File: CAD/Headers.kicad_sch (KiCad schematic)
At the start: 62 parts, among them J1 SWD, J10 OUT_0, J11 OUT_1, J12 OUT_2, J13 TEMP_0, J14 TEMP_1, J15 TEMP_2, J16 EXPANSION, J17 ESP_DB, J18 250-502/000-006, J19 A2543WV-5P, J2 A2543WV-2P, J20 IO_1, J21 IO_2, J22 A2543WV-2P, J23 CAN_1_OUT, J24 DRIVER_2, J25 DRIVER_1, J26 DRIVER_0, J28 SPI_DB, J3 OUT_6, J30 LASER/VFD, J31 IO_3, J33 A2543WV-4P, J34 A2543WV-4P, J35 DRIVER_3, J36 DRIVER_4, J37 DRIVER_5, J38 CAN_0_OUT, J39 PANELDUE_SD, J4 OUT_7, J41 TEMP_3, J42 DS_LED, J44 IO_7_ISO_OUT, J47 IO_8_ISO_OUT, J48 SBC, J49 A2543WV-2P, J5 OUT_8, J50 EXT_5V_IN, J51 IO_4, J53 IO_5, J54 IO_6, J55 IO_7, J56 IO_8, J59 A2543WV-2P, J6 OUT_3, J60 A2543WV-2P, J61 IO_7_ISO_IN, J62 IO_8_ISO_IN, J7 OUT_4, J8 OUT_5

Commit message: Fix Part Name
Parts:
- J18: value 250-502/000-006 -> 250-202/000-006; footprint 3DPotter:CONN2_250-502&slash_000-006_WAG -> 3DPotter:CONN2_250-202&slash_000-006_WAG; LCSC (none) -> C2765061
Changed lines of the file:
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@@
 			)
 		)
-		(property "Value" "250-502/000-006"
+		(property "Value" "250-202/000-006"
 			(at 53.34 26.6699 0)
 			(effects
@@
 			)
 		)
-		(property "Footprint" "3DPotter:CONN2_250-502&slash_000-006_WAG"
+		(property "Footprint" "3DPotter:CONN2_250-202&slash_000-006_WAG"
 			(at 48.006 30.226 0)
 			(effects
@@
 			)
 		)
-		(property "Datasheet" "250-502/000-006"
+		(property "Datasheet" "250-202/000-006"
 			(at 48.514 34.29 0)
 			(effects
@@
 				)
 				(hide yes)
+			)
+		)
+		(property "LCSC" "C2765061"
+			(at 39.37 24.13 0)
+			(effects
+				(font
+					(size 1.524 1.524)
+				)
+				(hide yes)

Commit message: Wago confuses me
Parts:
- J18: value 250-202/000-006 -> 250-502/000-006; footprint 3DPotter:CONN2_250-202&slash_000-006_WAG -> 3DPotter:CONN2_250-502&slash_000-006_WAG; LCSC C2765061 -> C3309714
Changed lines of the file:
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@@
 			)
 		)
-		(property "Value" "250-202/000-006"
+		(property "Value" "250-502/000-006"
 			(at 53.34 26.6699 0)
 			(effects
@@
 			)
 		)
-		(property "Footprint" "3DPotter:CONN2_250-202&slash_000-006_WAG"
+		(property "Footprint" "3DPotter:CONN2_250-502&slash_000-006_WAG"
 			(at 48.006 30.226 0)
 			(effects
@@
 			)
 		)
-		(property "Datasheet" "250-202/000-006"
+		(property "Datasheet" "250-502/000-006"
 			(at 48.514 34.29 0)
 			(effects
@@
 			)
 		)
-		(property "LCSC" "C2765061"
+		(property "LCSC" "C3309714"
 			(at 39.37 24.13 0)
 			(effects

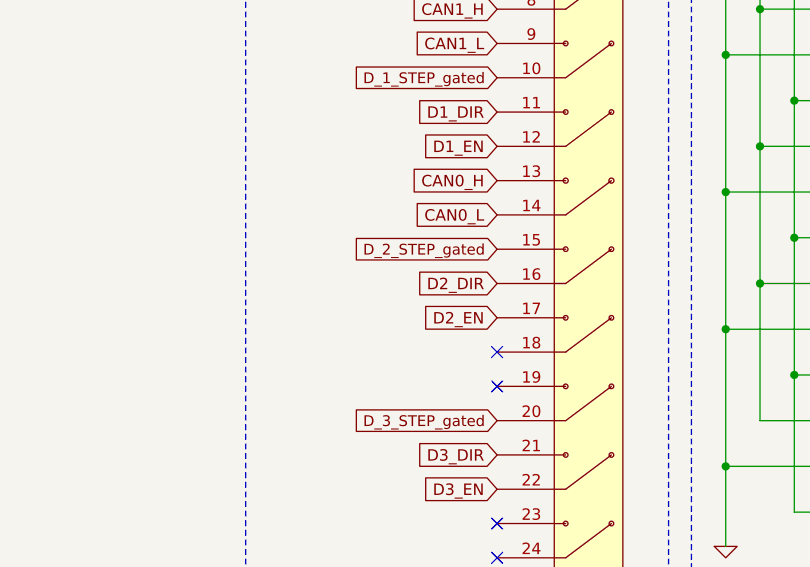
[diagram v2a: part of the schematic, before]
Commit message: Pin Changes / Misc
Changing some pins around so I have a chip select
Processor Pins:
PC28 ---> PA9 (Driver_2_Step)
PC29[AFE1_AD4] ---> PB1[AFE1_AD0] (TEMP_1)
PC28 -> spi1cs1
PC29 -> spi1cs2 (Unused as of now)
IDC Header:
CAN 0 Lines removed
13 -> SPI1_MOSI_BUFF
14 -> SP1_MISO
18 -> SPI1_SPCK_BUFF
19 -> spi1cs1
Misc:
Fixed all library links, should get a lot less errors now
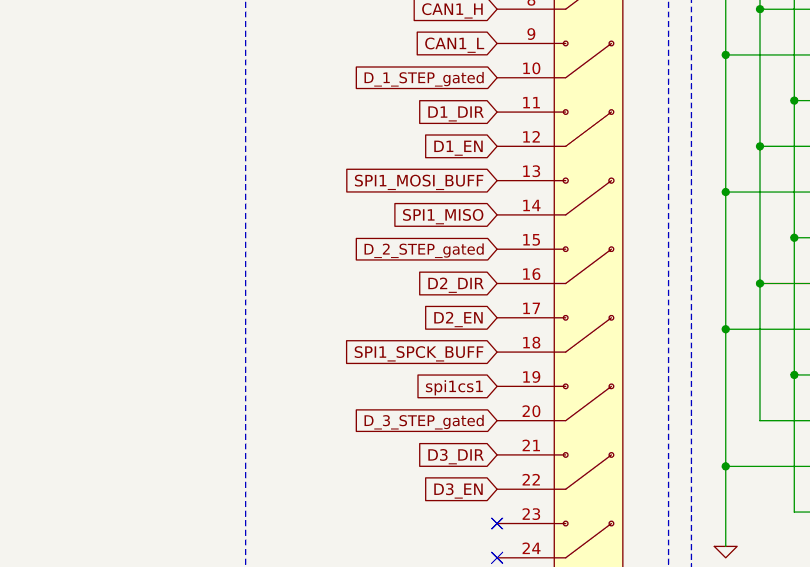
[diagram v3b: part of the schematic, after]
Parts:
- J19: footprint Connector_Molex:Wurth_61900511121-1x05_P2.54mm_Vertical(Molex_KK-254_AE-6410-05A_Compatibe) -> Connector_Molex:Molex_KK-254_AE-6410-05A_1x05_P2.54mm_Vertical
- J2, J49, J59, J60: footprint Connector_Molex:Wurth_61900211121-1x02_P2.54mm_Vertical-(Molex_KK-254_AE-6410-02Acompatible) -> Connector_Molex:Molex_KK-254_AE-6410-02A_1x02_P2.54mm_Vertical
- J30: footprint Connector_Molex:Wurth_61900311121-1x03_P2.54mm_Vertical(Molex_KK-254_AE-6410-03A_Compatible) -> Connector_Molex:Molex_KK-254_AE-6410-03A_1x03_P2.54mm_Vertical
- J33, J34: footprint Carters_Various_Bits_and_Pieces:Wurth_61900411121-1x04_P2.54mm_Vertical(1.2mm_ID) -> Connector_Molex:Molex_KK-254_AE-6410-04A_1x04_P2.54mm_Vertical
- R108: footprint Resistor_SMD:R_0603_1608Metric_Wbry -> Resistor_SMD:R_0603_1608Metric
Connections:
- net CAN0_H: no longer J16.13
- net CAN0_L: no longer J16.14
- net SPI1_MISO: now also J16.14
- net SPI1_MOSI_BUFF: now also J16.13
- net SPI1_SPCK_BUFF: now also J16.18
- net spi1cs1: now reaches J16.19
- no-connect marks 28 -> 26
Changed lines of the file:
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@@
 	)
 	(no_connect
-		(at 105.41 252.73)
-	)
-	(no_connect
 		(at 105.41 290.83)
 	)
@@
 		(at 208.915 65.405)
 	)
-	(no_connect
-		(at 105.41 256.54)
-	)
 	(wire
 		(pts
@@
 		)
 	)
+	(global_label "spi1cs1"
+		(shape input)
+		(at 105.41 256.54 180)
+		(effects
+			(font
+				(size 1.27 1.27)
+			)
+			(justify right)
+		)
+		(property "Intersheetrefs" "${INTERSHEET_REFS}"
+			(at 105.41 256.54 0)
+			(effects
+				(font
+					(size 1.27 1.27)
+				)
+				(hide yes)
+			)
+		)
+	)
 	(global_label "V_OUT_LC_1"
 		(shape input)
@@
 		)
 	)
-	(global_label "CAN0_L"
-		(shape input)
-		(at 105.41 237.49 180)
-		(fields_autoplaced yes)
-		(effects
-			(font
-				(size 1.27 1.27)
-			)
-			(justify right)
-		)
-		(property "Intersheetrefs" "${INTERSHEET_REFS}"
-			(at 96.1847 237.49 0)
-			(effects
-				(font
-					(size 1.27 1.27)
-				)
-				(justify right)
-				(hide yes)
-			)
-		)
-	)
 	(global_label "OUT_3_NEG"
 		(shape input)
@@
 		)
 	)
+	(global_label "SPI1_MISO"
+		(shape input)
+		(at 105.41 237.49 180)
+		(fields_autoplaced yes)
+		(effects
+			(font
+				(size 1.27 1.27)
+			)
+			(justify right)
+		)
+		(property "Intersheetrefs" "${INTERSHEET_REFS}"
+			(at 93.2214 237.49 0)
+			(effects
+				(font
+					(size 1.27 1.27)
+				)
+				(justify right)
+				(hide yes)
+			)
+		)
+	)
 	(global_label "D_0_ERR"
 		(shape input)
@@
 		)
 	)
+	(global_label "SPI1_MOSI_BUFF"
+		(shape input)
+		(at 105.41 233.68 180)
+		(fields_autoplaced yes)
+		(effects
+			(font
+				(size 1.27 1.27)
+			)
+			(justify right)
+		)
+		(property "Intersheetrefs" "${INTERSHEET_REFS}"
+			(at 87.4761 233.68 0)
+			(effects
+				(font
+					(size 1.27 1.27)
+				)
+				(justify right)
+				(hide yes)
+			)
+		)
+	)
 	(global_label "5V_EXT"
 		(shape input)
@@
 		)
 	)
-	(global_label "CAN0_H"
-		(shape input)
-		(at 105.41 233.68 180)
-		(fields_autoplaced yes)
-		(effects
-			(font
-				(size 1.27 1.27)
-			)
-			(justify right)
-		)
-		(property "Intersheetrefs" "${INTERSHEET_REFS}"
-			(at 95.8823 233.68 0)
-			(effects
-				(font
-					(size 1.27 1.27)
-				)
-				(justify right)
-				(hide yes)
-			)
-		)
-	)
 	(global_label "5V_EXT"
 		(shape input)
@@
 		)
 	)
+	(global_label "SPI1_SPCK_BUFF"
+		(shape input)
+		(at 105.41 252.73 180)
+		(fields_autoplaced yes)
+		(effects
+			(font
+				(size 1.27 1.27)
+			)
+			(justify right)
+		)
+		(property "Intersheetrefs" "${INTERSHEET_REFS}"
+			(at 87.0528 252.73 0)
+			(effects
+				(font
+					(size 1.27 1.27)
+				)
+				(justify right)
+				(hide yes)
+			)
+		)
+	)
 	(global_label "5V_EXT"
 		(shape input)
@@
 			)
 		)
-		(property "Footprint" "Connector_Molex:Wurth_61900211121-1x02_P2.54mm_Vertical-(Molex_KK-254_AE-6410-02Acompatible)"
+		(property "Footprint" "Connector_Molex:Molex_KK-254_AE-6410-02A_1x02_P2.54mm_Vertical"
 			(at 42.545 81.28 0)
 			(effects
@@
 			)
 		)
-		(property "Footprint" "Connector_Molex:Wurth_61900511121-1x05_P2.54mm_Vertical(Molex_KK-254_AE-6410-05A_Compatibe)"
+		(property "Footprint" "Connector_Molex:Molex_KK-254_AE-6410-05A_1x05_P2.54mm_Vertical"
 			(at 165.1 143.51 0)
 			(effects
@@
 			)
 		)
-		(property "Footprint" "Connector_Molex:Wurth_61900311121-1x03_P2.54mm_Vertical(Molex_KK-254_AE-6410-03A_Compatible)"
+		(property "Footprint" "Connector_Molex:Molex_KK-254_AE-6410-03A_1x03_P2.54mm_Vertical"
 			(at 58.42 165.735 0)
 			(effects
@@
 			)
 		)
-		(property "Footprint" "Resistor_SMD:R_0603_1608Metric_Wbry"
+		(property "Footprint" "Resistor_SMD:R_0603_1608Metric"
 			(at 46.99 162.56 0)
 			(effects
@@
 			)
 		)
-		(property "Footprint" "Connector_Molex:Wurth_61900211121-1x02_P2.54mm_Vertical-(Molex_KK-254_AE-6410-02Acompatible)"
+		(property "Footprint" "Connector_Molex:Molex_KK-254_AE-6410-02A_1x02_P2.54mm_Vertical"
 			(at 45.72 184.15 0)
 			(effects
@@
 			)
 		)
-		(property "Footprint" "Connector_Molex:Wurth_61900211121-1x02_P2.54mm_Vertical-(Molex_KK-254_AE-6410-02Acompatible)"
+		(property "Footprint" "Connector_Molex:Molex_KK-254_AE-6410-02A_1x02_P2.54mm_Vertical"
 			(at 201.93 104.14 0)
 			(effects
@@
 			)
 		)
-		(property "Footprint" "Connector_Molex:Wurth_61900211121-1x02_P2.54mm_Vertical-(Molex_KK-254_AE-6410-02Acompatible)"
+		(property "Footprint" "Connector_Molex:Molex_KK-254_AE-6410-02A_1x02_P2.54mm_Vertical"
 			(at 201.295 118.11 0)
 			(effects
@@
 			)
 		)
-		(property "Footprint" "Carters_Various_Bits_and_Pieces:Wurth_61900411121-1x04_P2.54mm_Vertical(1.2mm_ID)"
+		(property "Footprint" "Connector_Molex:Molex_KK-254_AE-6410-04A_1x04_P2.54mm_Vertical"
 			(at 238.125 100.965 0)
 			(effects
@@
 			)
 		)
-		(property "Footprint" "Carters_Various_Bits_and_Pieces:Wurth_61900411121-1x04_P2.54mm_Vertical(1.2mm_ID)"
+		(property "Footprint" "Connector_Molex:Molex_KK-254_AE-6410-04A_1x04_P2.54mm_Vertical"
 			(at 238.125 114.935 0)
 			(effects

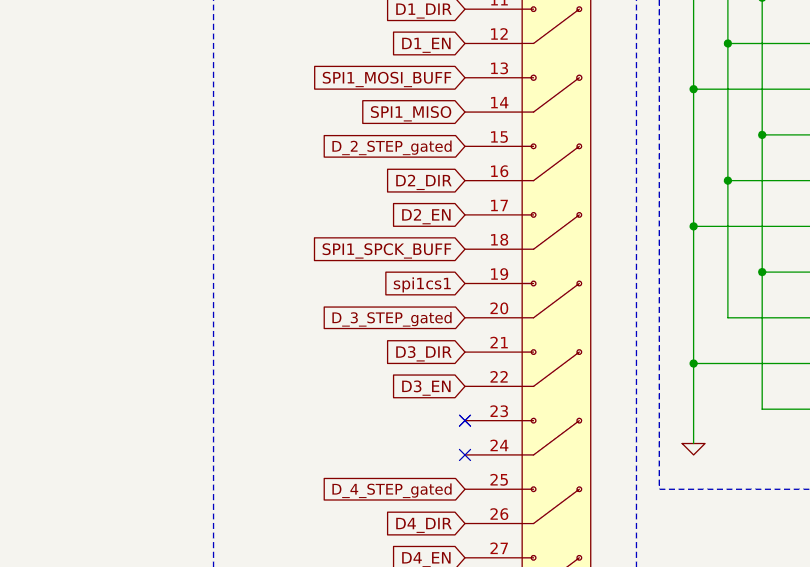
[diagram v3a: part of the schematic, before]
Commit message: Board Finished
Board has been slightly modified to add SPI to the BBC.
A lot of library mismatch/ not found errors were fixed. Only errors that exist currently are all related to the silkscreen edges on all 0402 components.
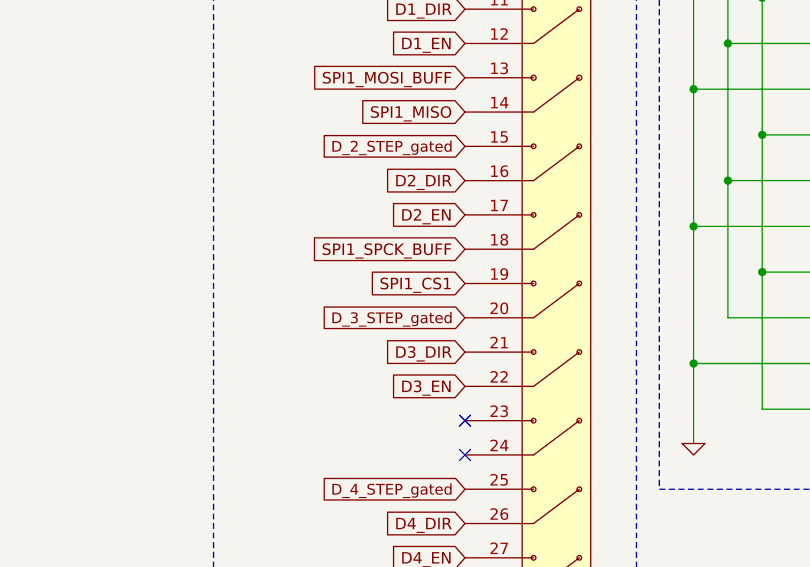
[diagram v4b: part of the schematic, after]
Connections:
- net spi1cs1 renamed SPI1_CS1
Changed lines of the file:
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@@
-		)
-	)
-	(global_label "spi1cs1"
-		(shape input)
-		(at 105.41 256.54 180)
-		(effects
-			(font
-				(size 1.27 1.27)
-			)
-			(justify right)
-		)
-		(property "Intersheetrefs" "${INTERSHEET_REFS}"
-			(at 105.41 256.54 0)
-			(effects
-				(font
-					(size 1.27 1.27)
-				)
-				(hide yes)
-			)
 		)
 	)
@@
 			(effects
 				(font
+					(size 1.27 1.27)
+				)
+				(justify right)
+				(hide yes)
+			)
+		)
+	)
+	(global_label "SPI1_CS1"
+		(shape input)
+		(at 105.41 256.54 180)
+		(fields_autoplaced yes)
+		(effects
+			(font
+				(size 1.27 1.27)
+			)
+			(justify right)
+		)
+		(property "Intersheetrefs" "${INTERSHEET_REFS}"
+			(at 94.1286 256.54 0)
+			(effects
+				(font

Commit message: V1.55 Pre Maufacturing
Final change for 1.55, changed connectors to jst due to board height issues with the stepper boards
DFM passed
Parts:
- removed J30: LASER/VFD, Connector_Molex:Molex_KK-254_AE-6410-03A_1x03_P2.54mm_Vertical, symbol Connector_Generic:Conn_01x03
- removed J49: A2543WV-2P, Connector_Molex:Molex_KK-254_AE-6410-02A_1x02_P2.54mm_Vertical, symbol Connector_Generic:Conn_01x02
- removed R108: 100R, Resistor_SMD:R_0603_1608Metric, symbol Device:R_Small
- removed TP16: VFD, TestPoint:TestPoint_Pad_D1.5mm, symbol Duet3:TP
- added JP1: ERASE, Connector_PinHeader_2.54mm:PinHeader_1x02_P2.54mm_Vertical, symbol Device:Jumper
- J19: footprint Connector_Molex:Molex_KK-254_AE-6410-05A_1x05_P2.54mm_Vertical -> Connector_JST:JST_XH_B5B-XH-A_1x05_P2.50mm_Vertical; LCSC C239365 -> C157991; Part Number A2543WV-5P -> B5B-XH-A(LF)(SN)
- J2, J59, J60: footprint Connector_Molex:Molex_KK-254_AE-6410-02A_1x02_P2.54mm_Vertical -> Connector_JST:JST_XH_B2B-XH-A_1x02_P2.50mm_Vertical; LCSC C239362 -> C158012; Part Number A2543WV-2P -> B2B-XH-A(LF)(SN)
- J33, J34: footprint Connector_Molex:Molex_KK-254_AE-6410-04A_1x04_P2.54mm_Vertical -> Connector_JST:JST_XH_B4B-XH-A_1x04_P2.50mm_Vertical; LCSC C239364 -> C144395; Part Number A2543WV-4P -> B4B-XH-A(LF)(SN)
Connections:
- net GND: now also JP1.1
- net RESET_EXT: now also JP1.2
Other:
- moved on the sheet: J22

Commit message: Update Revision 1.56
1.56 Should be production board that is going on all scara* and cartesian printers. 1.56 is a final check that everything is silkscreened properly and all connectors are the correct ones.
*Not all scaras. Only scara that does not have this board should be Jarret Gross' scara
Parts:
- JP1: value ERASE -> RESET
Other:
- note added: "Before Next Order Change to KK-254"
- moved on the sheet: JP1
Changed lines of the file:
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@@
 		)
 	)
+	(text "Before Next Order Change to KK-254\n"
+		(exclude_from_sim no)
+		(at 44.45 78.74 0)
+		(effects
+			(font
+				(size 1.524 1.524)
+			)
+		)
+	)
 	(text "PanelDue"
 		(exclude_from_sim no)
@@
 	(wire
 		(pts
-			(xy 35.56 185.42) (xy 45.72 185.42)
+			(xy 35.56 185.42) (xy 44.45 185.42)
 		)
 		(stroke
@@
 	(wire
 		(pts
-			(xy 45.72 170.18) (xy 24.13 170.18)
+			(xy 44.45 170.18) (xy 24.13 170.18)
 		)
 		(stroke
@@
 	(symbol
 		(lib_id "Device:Jumper")
-		(at 45.72 177.8 270)
+		(at 44.45 177.8 270)
 		(unit 1)
 		(exclude_from_sim no)
@@
 		(dnp no)
 		(property "Reference" "JP1"
-			(at 48.9458 176.6316 90)
+			(at 47.6758 176.6316 90)
 			(effects
 				(font
@@
 			)
 		)
-		(property "Value" "ERASE"
-			(at 48.9458 178.943 90)
+		(property "Value" "RESET"
+			(at 47.6758 178.943 90)
 			(effects
 				(font
@@
 		)
 		(property "Footprint" "Connector_PinHeader_2.54mm:PinHeader_1x02_P2.54mm_Vertical"
-			(at 45.72 177.8 0)
+			(at 44.45 177.8 0)
 			(effects
 				(font
@@
 		)
 		(property "Datasheet" "~"
-			(at 45.72 177.8 0)
+			(at 44.45 177.8 0)
 			(effects
 				(font
@@
 		)
 		(property "Description" ""
-			(at 45.72 177.8 0)
+			(at 44.45 177.8 0)
 			(effects
 				(font
@@
 		)
 		(property "Part Number" "PZ254V-11-02P"
-			(at 45.72 177.8 0)
+			(at 44.45 177.8 0)
 			(effects
 				(font
@@
 		)
 		(property "LCSC" "C492401"
-			(at 45.72 177.8 90)
+			(at 44.45 177.8 90)
 			(effects
 				(font
@@
 		)
 		(property "RotOffset" "90"
-			(at 45.72 177.8 90)
+			(at 44.45 177.8 90)
 			(effects
 				(font

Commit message: Finalize changes for 1.56
LCSC and P/N updated for excessively out of stock parts.
Silkscreen changes so no more DRC errors
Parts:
- J2: footprint Connector_JST:JST_XH_B2B-XH-A_1x02_P2.50mm_Vertical -> Connector_Molex:Molex_KK-254_AE-6410-02A_1x02_P2.54mm_Vertical; LCSC C158012 -> C239362; Part Number B2B-XH-A(LF)(SN) -> A2543WV-2P
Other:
- note removed: "Before Next Order Change to KK-254"
- title: Duet 3 Main Board 3DP -> Duet 3 MB 3DP
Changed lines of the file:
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@@
 	(paper "A3" portrait)
 	(title_block
-		(title "Duet 3 Main Board 3DP")
-		(date "2026-02-17")
-		(rev "1.55")
+		(title "Duet 3 MB 3DP")
+		(date "2026-06-02")
+		(rev "1.56")
 		(company "3DPotter")
 		(comment 1 "(c) 3DPotter")
@@
 		)
 	)
-	(text "Before Next Order Change to KK-254\n"
-		(exclude_from_sim no)
-		(at 44.45 78.74 0)
-		(effects
-			(font
-				(size 1.524 1.524)
-			)
-		)
-	)
 	(text "PanelDue"
 		(exclude_from_sim no)
@@
 			)
 		)
-		(property "Footprint" "Connector_JST:JST_XH_B2B-XH-A_1x02_P2.50mm_Vertical"
+		(property "Footprint" "Connector_Molex:Molex_KK-254_AE-6410-02A_1x02_P2.54mm_Vertical"
 			(at 42.545 81.28 0)
 			(effects
@@
 			)
 		)
-		(property "Part Number" "B2B-XH-A(LF)(SN)"
+		(property "Part Number" "A2543WV-2P"
 			(at 42.545 81.28 0)
 			(effects
@@
 			)
 		)
-		(property "LCSC" "C158012"
+		(property "LCSC" "C239362"
 			(at 42.545 81.28 0)
 			(effects

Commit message: Forgot to save
Same changes as last commit, I forgot to save before pushing
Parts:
- TP39: footprint TestPoint:TestPoint_Pad_D1.5mm -> 3DPotter:TestPoint_Pad_D1.5mm
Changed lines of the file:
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@@
 			)
 		)
-		(property "Footprint" "TestPoint:TestPoint_Pad_D1.5mm"
+		(property "Footprint" "3DPotter:TestPoint_Pad_D1.5mm"
 			(at 258.445 24.765 0)
 			(effects
